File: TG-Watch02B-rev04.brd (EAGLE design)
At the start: 36.8 x 40.6 mm, 62 parts, among them IC3 W25Q128JVSIQ TR, Q3 DMG2305, U10 MCU-ATTINY10, U2 BQ27441-G1, U4 FAN5331SX, U7 DISP_1.54_LCMTF15423A-C_LCD+C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, U8 UNDERVOLT-TPS3702CX3, U9 MCP73831/OT

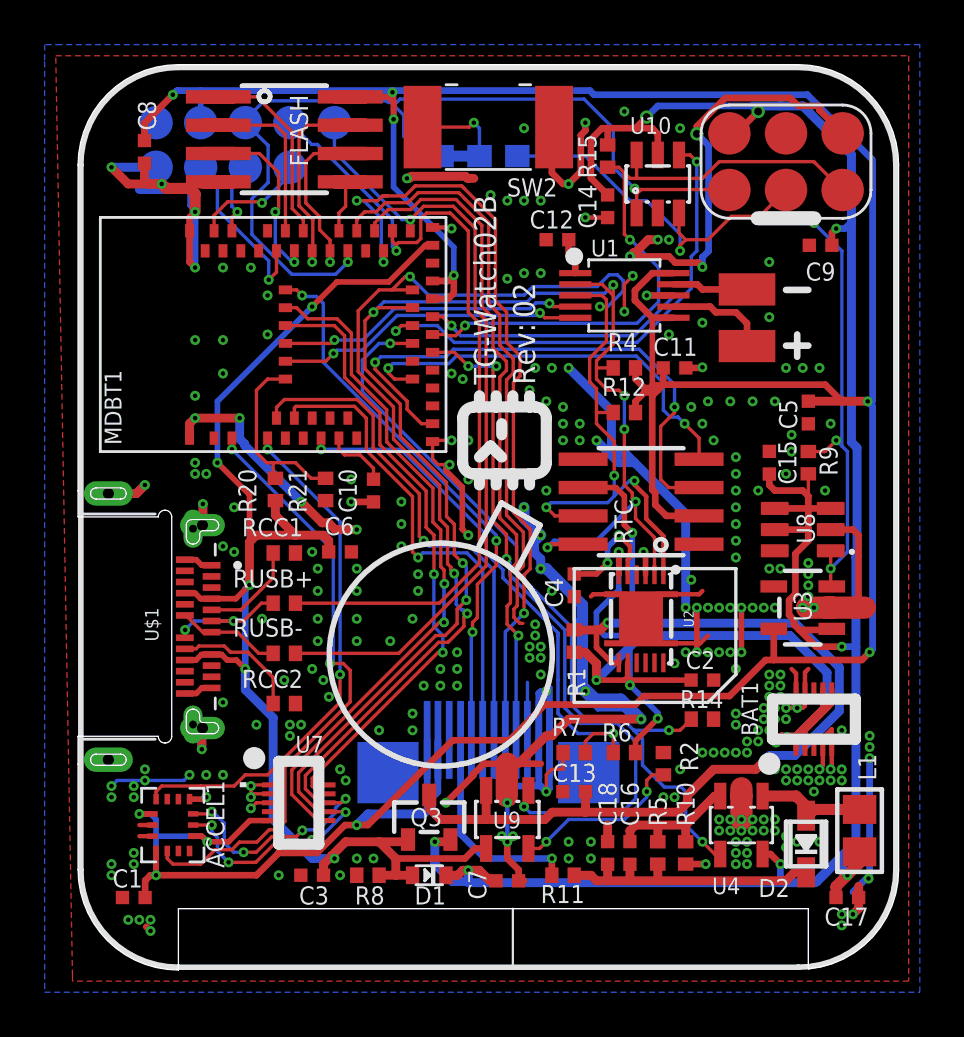
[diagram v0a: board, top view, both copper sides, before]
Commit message: chagne battery IC and make path for rev02 boards
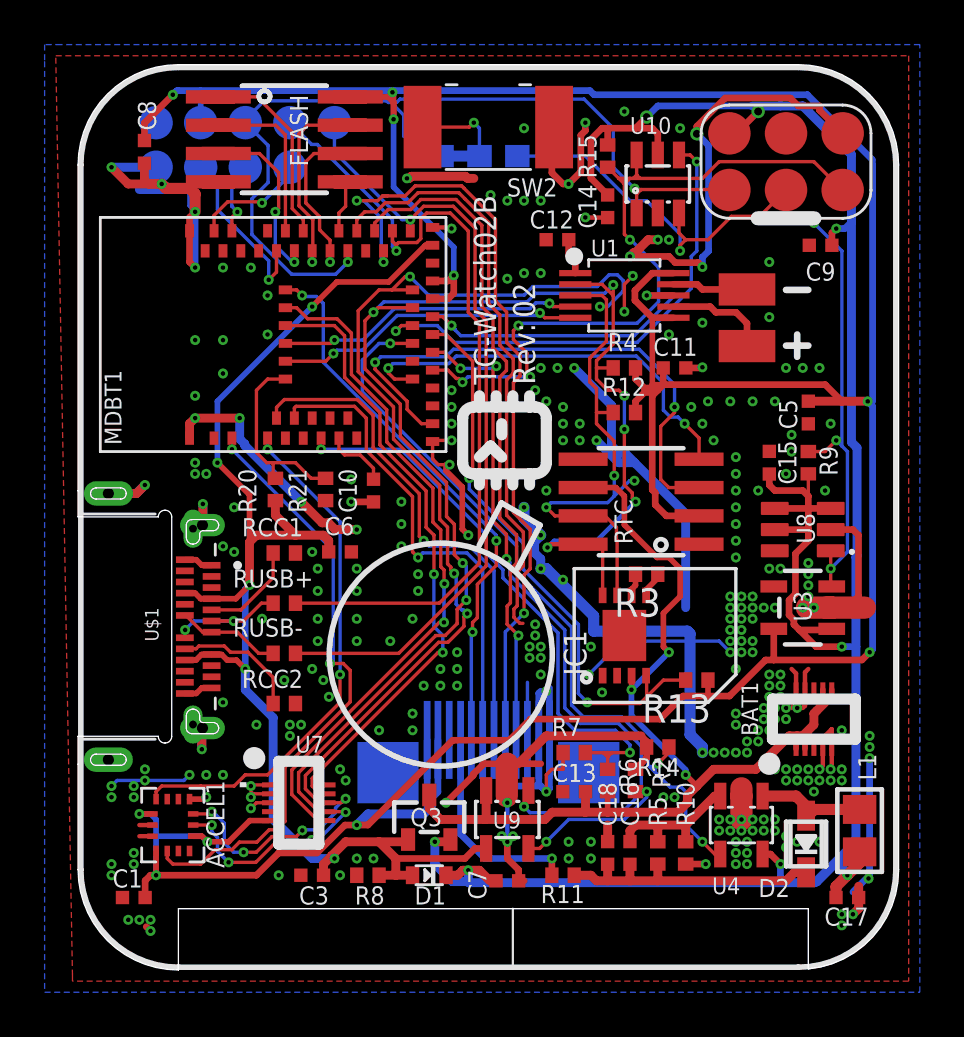
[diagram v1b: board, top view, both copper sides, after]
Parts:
- removed C2, C4: 1uf, 0TG-Lib v01.5:MICROBUILDER__0402_NODIMS
- removed R1: .01 ohm, 0TG-Lib v01.5:TG_0402
- removed U2: BQ27441-G1, battery-management-temp:PDSO-N12
- added IC1: LC709203F, microbuilder:WDFN8_3X4_0.65
- added R13: 10k, 0TG-Lib v01.5:TG_0402
- added R3: 11k, 0TG-Lib v01.5:TG_0402
- moved R14 2.36 mm to (26.0, 10.0), turned to 0 degrees
- moved R2 1.46 mm to (25.0, 8.50)
- moved R6 1.46 mm to (23.8, 8.50), turned to 270 degrees
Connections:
- removed net 1.8V: C4.2, U2.5
- removed net A0: MDBT1.20
- removed net D12_SMC_RESET: ISP1.5, MDBT1.24, R15.2, U10.6
- removed net GPOUT: U2.12
- removed net TS: U2.10
- removed net VBAT_RAW: BAT1.P$1, BAT1.P$2, BAT1.P$6, BAT1.P$7, C2.2, R1.2, R6.2, U2.6, U2.8
- new net A0_SMC_RESET: ISP1.5, MDBT1.20, R15.2, U10.6
- new net D12_BAT_INT: IC1.4, MDBT1.24, R13.2
- new net TSENSE: IC1.6, R3.2
- new net TSW: IC1.5, R3.1
- net 3V3: now also R13.1
- net GND: now also IC1.1, IC1.2; no longer C2.1, C4.1, U2.3, U2.EP, U2.EP1, U2.EP2, U2.EP3, U2.EP4
- net SCL: now also IC1.8; no longer U2.2
- net SDA: now also IC1.7; no longer U2.1
- net VBAT: now also BAT1.P$1, BAT1.P$2, BAT1.P$6, BAT1.P$7, IC1.3, R6.2; no longer R1.1, U2.7
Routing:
- net VBAT_RAW: track 45.8 -> 0.00 mm, vias 6 -> 0
- net A0_SMC_RESET: track 0.00 -> 35.4 mm, vias 0 -> 4
- net D12_SMC_RESET: track 31.2 -> 0.00 mm, vias 2 -> 0
- net D12_BAT_INT: track 0.00 -> 25.6 mm, vias 0 -> 2
- net GND: track 196.0 -> 189.3 mm
- net 1.8V: track 5.18 -> 0.00 mm, vias 2 -> 0
- net VDIV: track 24.4 -> 26.3 mm
- net VBAT: track 48.7 -> 47.3 mm
- net D6_BACKLIGHT: track 35.7 -> 34.4 mm
- net TSW: track 0.00 -> 1.17 mm
- net TSENSE: track 0.00 -> 1.02 mm
- net BAT_CHRG_SET: track 7.86 -> 7.01 mm
- net 3V3: track 166.8 -> 167.6 mm
